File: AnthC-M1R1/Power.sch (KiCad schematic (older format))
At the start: 30 parts, among them Q8 SI2347DS-T1-GE3, Q9 SI2347DS-T1-GE3, U1 TPS54331DR, U3 TPS78533

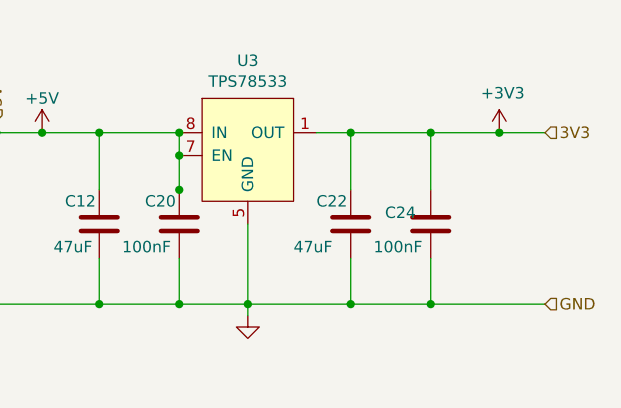
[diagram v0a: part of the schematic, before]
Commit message: Placement continued. Replaced quadrupled TVS by double ones to make routing easier
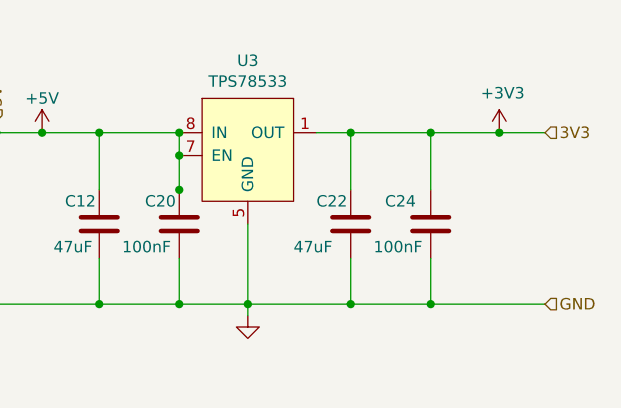
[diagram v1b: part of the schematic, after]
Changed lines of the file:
@@
 AR Path="/6251F79F" Ref="C?"  Part="1"
 AR Path="/6243F6D9/6251F79F" Ref="C24"  Part="1"
-F 0 "C24" H 9300 2050 50  0000 L CNN
+F 0 "C24" H 9300 2100 50  0000 L CNN
 F 1 "100nF" H 9250 1900 50  0000 L CNN
 F 2 "Capacitor_SMD:C_0603_1608Metric" H 10900 2200 50  0001 C CNN

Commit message: Placement continued
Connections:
- net GND: now also R2.2; no longer C7.2
- net at C5.1, U1.6 (COMP): now also C7.1; no longer R2.1
- new net: C7.2, R2.1
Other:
- moved on the sheet: C7, R2
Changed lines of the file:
@@
 AR Path="/6269B46A" Ref="R?"  Part="1"
 AR Path="/6243F6D9/6269B46A" Ref="R86"  Part="1"
-F 0 "R86" V 5800 2350 50  0000 L CNN
+F 0 "R86" V 5700 2300 50  0000 L CNN
 F 1 "8.2KΩ" H 5900 2300 50  0000 C CNN
 F 2 "Resistor_SMD:R_0603_1608Metric" H 5700 3350 50  0001 C CNN
@@
 L Resistor_0603:49.9 R?
 U 1 1 6269B4DA
-P 3600 2100
+P 3600 2300
 AR Path="/602E71BC/6269B4DA" Ref="R?"  Part="1"
 AR Path="/6269B4DA" Ref="R?"  Part="1"
 AR Path="/6243F6D9/6269B4DA" Ref="R2"  Part="1"
-F 0 "R2" H 3650 2200 50  0000 L CNN
-F 1 "49.9" H 3750 2050 50  0000 C CNN
-F 2 "Resistor_SMD:R_0603_1608Metric" H 3600 3100 50  0001 C CNN
-F 3 "https://www.mouser.be/datasheet/2/427/VISH_S_A0011410627_1-2571984.pdf" V 3250 2150 50  0001 C CNN
-F 4 "Vishay" H 3600 3425 50  0001 C CNN "Manufacturer"
-F 5 "33 kOhms ±1% 0.1W, 1/10W Chip Resistor 0603 (1608 Metric) Moisture Resistant Thick Film" H 3600 3025 50  0001 C CNN "Description"
-F 6 "TNPW020149R9BEED" H 3600 3225 50  0001 C CNN "Manufacturer Nr."
-F 7 "75mW" H 3600 3500 50  0001 C CNN "Power"
-F 8 "0.09" H 3600 2925 50  0001 C CNN "Price"
-F 9 "Mouser" H 3600 3325 50  0001 C CNN "Supplier"
-F 10 "71-TNPW020149R9BEED" H 3600 3625 50  0001 C CNN "Supplier Nr."
-F 11 "1%" H 3600 2850 50  0001 C CNN "Tolerance"
-F 12 "TNPW020149R9BEED" H 3600 2100 50  0001 C CNN "MPN"
-	1    3600 2100
+F 0 "R2" H 3650 2400 50  0000 L CNN
+F 1 "49.9" H 3750 2250 50  0000 C CNN
+F 2 "Resistor_SMD:R_0603_1608Metric" H 3600 3300 50  0001 C CNN
+F 3 "https://www.mouser.be/datasheet/2/427/VISH_S_A0011410627_1-2571984.pdf" V 3250 2350 50  0001 C CNN
+F 4 "Vishay" H 3600 3625 50  0001 C CNN "Manufacturer"
+F 5 "33 kOhms ±1% 0.1W, 1/10W Chip Resistor 0603 (1608 Metric) Moisture Resistant Thick Film" H 3600 3225 50  0001 C CNN "Description"
+F 6 "TNPW020149R9BEED" H 3600 3425 50  0001 C CNN "Manufacturer Nr."
+F 7 "75mW" H 3600 3700 50  0001 C CNN "Power"
+F 8 "0.09" H 3600 3125 50  0001 C CNN "Price"
+F 9 "Mouser" H 3600 3525 50  0001 C CNN "Supplier"
+F 10 "71-TNPW020149R9BEED" H 3600 3825 50  0001 C CNN "Supplier Nr."
+F 11 "1%" H 3600 3050 50  0001 C CNN "Tolerance"
+F 12 "TNPW020149R9BEED" H 3600 2300 50  0001 C CNN "MPN"
+	1    3600 2300
 	1    0    0    -1
 $EndComp
@@
 L Device:C_Small C?
 U 1 1 6269B4E3
-P 3600 2350
+P 3600 2050
 AR Path="/602E71BC/6269B4E3" Ref="C?"  Part="1"
 AR Path="/6269B4E3" Ref="C?"  Part="1"
 AR Path="/6243F6D9/6269B4E3" Ref="C7"  Part="1"
-F 0 "C7" H 3692 2396 50  0000 L CNN
-F 1 "4.7nF" H 3692 2305 50  0000 L CNN
-F 2 "Capacitor_SMD:C_0402_1005Metric" H 3600 2350 50  0001 C CNN
-F 3 "~" H 3600 2350 50  0001 C CNN
-F 4 "C1538" H 3600 2350 50  0001 C CNN "LCSC-PN"
-F 5 "0402B472K500NT" H 3600 2350 50  0001 C CNN "MPN"
-F 6 "Guangdong Fenghua Advanced Tech" H 3600 2350 50  0001 C CNN "Manufacturer"
-	1    3600 2350
-	1    0    0    -1
-$EndComp
+F 0 "C7" H 3692 2096 50  0000 L CNN
+F 1 "4.7nF" H 3692 2005 50  0000 L CNN
+F 2 "Capacitor_SMD:C_0402_1005Metric" H 3600 2050 50  0001 C CNN
+F 3 "~" H 3600 2050 50  0001 C CNN
+F 4 "C1538" H 3600 2050 50  0001 C CNN "LCSC-PN"
+F 5 "0402B472K500NT" H 3600 2050 50  0001 C CNN "MPN"
+F 6 "Guangdong Fenghua Advanced Tech" H 3600 2050 50  0001 C CNN "Manufacturer"
+	1    3600 2050
+	1    0    0    -1
+$EndComp

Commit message: Placement continued
Replaced L1 by another inductance that supports 3A
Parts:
- L1: value 10μH -> 10μH-5A; footprint Inductors:Inductor_Wurth_LQS-4025 -> Inductors:Inductor_Wurth_XHMI-6060; symbol Inductors:10μH -> Inductors:10μH-5A; MPN 74404043100A -> 74439346100; Price 0.435 -> (none); Supplier Part Number 710-74404043100A -> 710-74439346100
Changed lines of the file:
@@
 $EndComp
 $Comp
-L Inductors:10μH L?
+L Inductors:10μH-5A L?
 U 1 1 6269B54A
 P 5000 1600
@@
 AR Path="/6243F6D9/6269B54A" Ref="L1"  Part="1"
 F 0 "L1" V 5190 1600 50  0000 C CNN
-F 1 "10μH" V 5075 1600 50  0000 C CNN
-F 2 "Inductors:Inductor_Wurth_LQS-4025" H 5000 1600 50  0001 C CNN
-F 3 "https://www.we-online.com/catalog/datasheet/74404043100A.pdf" H 5000 1600 50  0001 C CNN
-F 4 "74404043100A" H 6200 2050 50  0001 C CNN "MPN"
+F 1 "10μH-5A" V 5075 1600 50  0000 C CNN
+F 2 "Inductors:Inductor_Wurth_XHMI-6060" H 5000 1600 50  0001 C CNN
+F 3 "https://www.we-online.com/catalog/datasheet/74439346100.pdf" H 5000 1600 50  0001 C CNN
+F 4 "74439346100" H 6200 2050 50  0001 C CNN "MPN"
 F 5 "Wurth Elektronik" H 5500 2050 50  0001 C CNN "Manufacturer"
-F 6 "0.435" H 5350 1850 50  0001 C CNN "Price"
-F 7 "Mouser" H 5350 1950 50  0001 C CNN "Supplier"
-F 8 "710-74404043100A" H 6300 1950 50  0001 C CNN "Supplier Part Number"
+F 6 "Mouser" H 5350 1950 50  0001 C CNN "Supplier"
+F 7 "710-74439346100" H 6300 1950 50  0001 C CNN "Supplier Part Number"
 	1    5000 1600
 	0    -1   -1   0

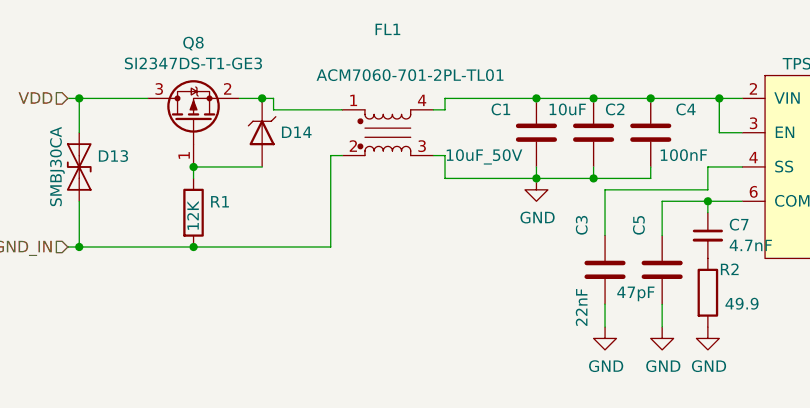
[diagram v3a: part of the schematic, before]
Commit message: Routing continued Changed the order of the connector J5 to improve routing
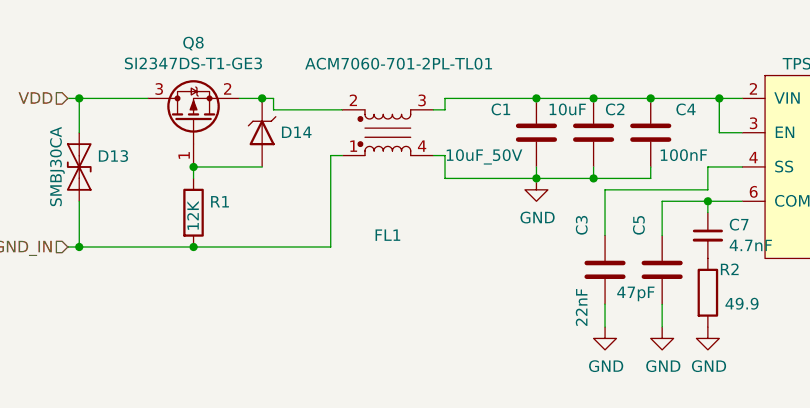
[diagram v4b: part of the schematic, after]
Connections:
- net GND: now also FL1.4; no longer FL1.3
- net GND_IN: now also FL1.1; no longer FL1.2
- net at D14.1 (K), Q8.2 (S): now also FL1.2; no longer FL1.1
- net at C1.1, C2.1, C4.1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: now also FL1.3; no longer FL1.4
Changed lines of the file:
@@
 L Inductors:ACM7060-701-2PL-TL01 FL1
 U 1 1 6236793A
-P 2000 1700
-F 0 "FL1" H 2200 2250 50  0000 C CNN
-F 1 "ACM7060-701-2PL-TL01" H 2300 2050 50  0000 C CNN
-F 2 "Inductors:ChokeSMD_ACM7060" H 2000 3050 50  0001 C CNN
-F 3 "https://product.tdk.com/system/files/dam/doc/product/emc/emc/cmf_cmc/catalog/cmf_commercial_power_acm7060_en.pdf" V 2200 1760 50  0001 C CNN
-F 4 "Common Mode Chokes / Filters 700ohms 100MHz 50volts" H 2000 2950 50  0001 C CNN "Description"
-F 5 "TDK" H 2000 2850 50  0001 C CNN "Manufacturer"
-F 6 "ACM7060-701-2PL-TL01" H 2000 2750 50  0001 C CNN "Manufacturer Nr."
-F 7 "Mouser" H 2000 2650 50  0001 C CNN "Supplier"
-F 8 "810-ACM70607012PLTL1" H 2000 2550 50  0001 C CNN "Supplier Nr."
-	1    2000 1700
-	1    0    0    -1
+P 2000 1500
+F 0 "FL1" H 2200 2050 50  0000 C CNN
+F 1 "ACM7060-701-2PL-TL01" H 2250 1300 50  0000 C CNN
+F 2 "Inductors:ChokeSMD_ACM7060" H 2000 2850 50  0001 C CNN
+F 3 "https://product.tdk.com/system/files/dam/doc/product/emc/emc/cmf_cmc/catalog/cmf_commercial_power_acm7060_en.pdf" V 2200 1560 50  0001 C CNN
+F 4 "Common Mode Chokes / Filters 700ohms 100MHz 50volts" H 2000 2750 50  0001 C CNN "Description"
+F 5 "TDK" H 2000 2650 50  0001 C CNN "Manufacturer"
+F 6 "ACM7060-701-2PL-TL01" H 2000 2550 50  0001 C CNN "Manufacturer Nr."
+F 7 "Mouser" H 2000 2450 50  0001 C CNN "Supplier"
+F 8 "810-ACM70607012PLTL1" H 2000 2350 50  0001 C CNN "Supplier Nr."
+	1    2000 1500
+	1    0    0    1
 $EndComp
 Wire Wire Line

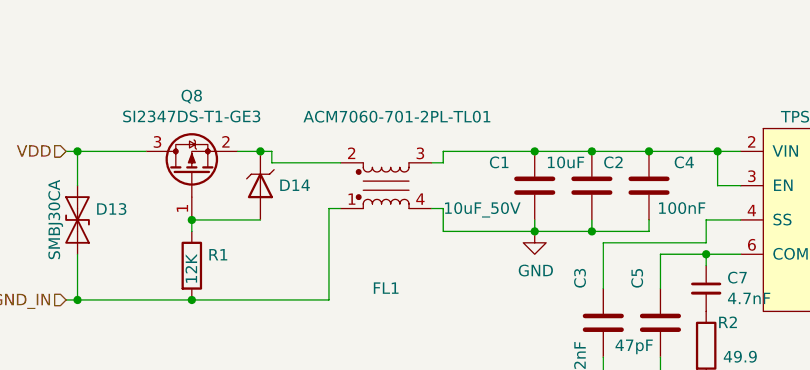
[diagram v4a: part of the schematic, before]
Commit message: Layout continued. Verified USB-C. Corrected layout of the TPS DC/DC converter
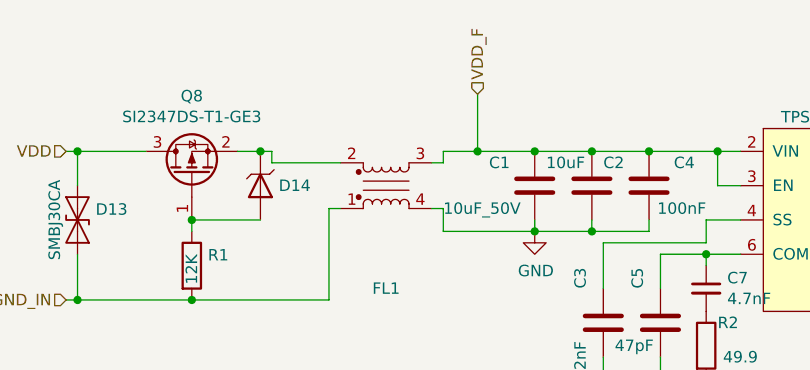
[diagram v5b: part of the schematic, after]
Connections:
- net VDD_F: now reaches C1.1, C2.1, C4.1, FL1.3, U1.2 (VIN), U1.3 (EN)
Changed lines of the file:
@@
 P 2000 1500
 F 0 "FL1" H 2200 2050 50  0000 C CNN
-F 1 "ACM7060-701-2PL-TL01" H 2250 1300 50  0000 C CNN
+F 1 "ACM7060-701-2PL-TL01" H 2250 1300 50  0001 C CNN
 F 2 "Inductors:ChokeSMD_ACM7060" H 2000 2850 50  0001 C CNN
 F 3 "https://product.tdk.com/system/files/dam/doc/product/emc/emc/cmf_cmc/catalog/cmf_commercial_power_acm7060_en.pdf" V 2200 1560 50  0001 C CNN
@@
 	2450 1500 2450 1450
 Wire Wire Line
-	2450 1450 2850 1450
+	2450 1450 2600 1450
 Wire Wire Line
 	2400 1500 2450 1500
@@
 Wire Wire Line
 	1350 2100 1950 2100
+Text HLabel 2600 1200 1    50   Input ~ 0
+VDD_F
+Wire Wire Line
+	2600 1450 2600 1200
+Connection ~ 2600 1450
+Wire Wire Line
+	2600 1450 2850 1450
 $EndSCHEMATC

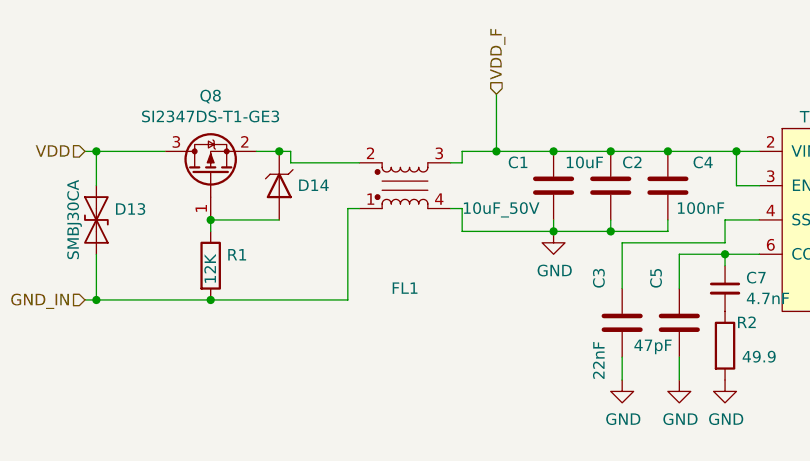
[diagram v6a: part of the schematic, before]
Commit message: Updated BOM info: added MPN to all the components
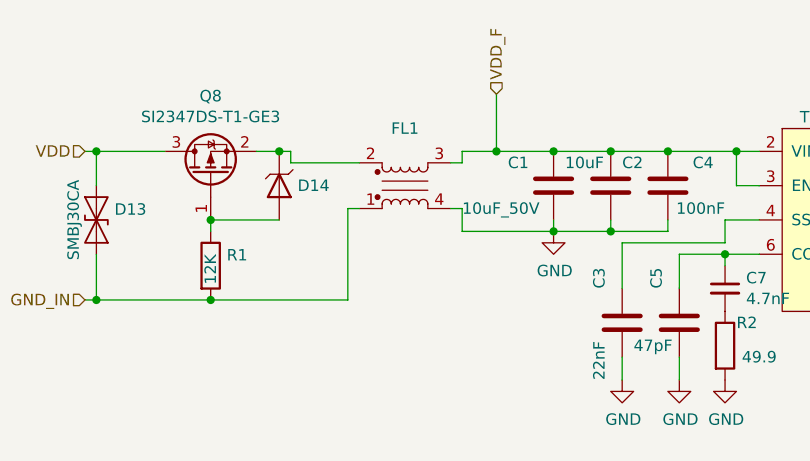
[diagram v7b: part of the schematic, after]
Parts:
- D13: MPN (none) -> SMBJ30CA; Manufacturer Part Number SMBJ30CA -> (none)
- D14, D24: MPN (none) -> MMSZ5233B-E3-08; Manufacturer Part Number MMSZ5233B-E3-08 -> (none)
- FL1: MPN (none) -> ACM7060-701-2PL-TL01; Manufacturer Nr. ACM7060-701-2PL-TL01 -> (none)
- Q8, Q9: MPN (none) -> SI2347DS-T1-GE3; Manufacturer Nr. SI2347DS-T1-GE3 -> (none)
- R1, R87: MPN (none) -> RT0603FRE0712KL; Manufacturer Part Number RT0603FRE0712KL -> (none)
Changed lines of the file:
@@
 F 4 "Suppresseurs ESD / diodes TVS 600W 30V 5% Bi-Directional" H 850 2900 50  0001 C CNN "Description"
 F 5 "Littelfuse" H 850 2800 50  0001 C CNN "Manufacturer"
-F 6 "SMBJ30CA" H 850 2700 50  0001 C CNN "Manufacturer Part Number"
-F 7 "Mouser" H 850 1750 50  0001 C CNN "Supplier"
-F 8 "576-SMBJ30CA" H 850 1750 50  0001 C CNN "Supplier Part Number"
+F 6 "Mouser" H 850 1750 50  0001 C CNN "Supplier"
+F 7 "576-SMBJ30CA" H 850 1750 50  0001 C CNN "Supplier Part Number"
+F 8 "SMBJ30CA" H 850 2700 50  0001 C CNN "MPN"
 	1    850  1750
 	0    1    1    0
@@
 U 1 1 6236793A
 P 2000 1500
-F 0 "FL1" H 2200 2050 50  0000 C CNN
+F 0 "FL1" H 2200 1350 50  0000 C CNN
 F 1 "ACM7060-701-2PL-TL01" H 2250 1300 50  0001 C CNN
 F 2 "Inductors:ChokeSMD_ACM7060" H 2000 2850 50  0001 C CNN
@@
 F 4 "Common Mode Chokes / Filters 700ohms 100MHz 50volts" H 2000 2750 50  0001 C CNN "Description"
 F 5 "TDK" H 2000 2650 50  0001 C CNN "Manufacturer"
-F 6 "ACM7060-701-2PL-TL01" H 2000 2550 50  0001 C CNN "Manufacturer Nr."
-F 7 "Mouser" H 2000 2450 50  0001 C CNN "Supplier"
-F 8 "810-ACM70607012PLTL1" H 2000 2350 50  0001 C CNN "Supplier Nr."
+F 6 "Mouser" H 2000 2450 50  0001 C CNN "Supplier"
+F 7 "810-ACM70607012PLTL1" H 2000 2350 50  0001 C CNN "Supplier Nr."
+F 8 "ACM7060-701-2PL-TL01" H 2000 1500 50  0001 C CNN "MPN"
 	1    2000 1500
 	1    0    0    1
@@
 F 4 "MOSFET -30V Vds 20V Vgs SOT-23" H 1350 2850 50  0001 C CNN "Description"
 F 5 "Vishay Semiconductors" H 1350 2750 50  0001 C CNN "Manufacturer"
-F 6 "SI2347DS-T1-GE3" H 1350 2650 50  0001 C CNN "Manufacturer Nr."
-F 7 "Mouser" H 1350 2550 50  0001 C CNN "Supplier"
-F 8 "78-SI2347DS-T1-GE3" H 1350 2450 50  0001 C CNN "Supplier Nr."
+F 6 "Mouser" H 1350 2550 50  0001 C CNN "Supplier"
+F 7 "78-SI2347DS-T1-GE3" H 1350 2450 50  0001 C CNN "Supplier Nr."
+F 8 "SI2347DS-T1-GE3" H 1350 1450 50  0001 C CNN "MPN"
 	1    1350 1450
 	0    -1   -1   0
@@
 F 3 "https://www.mouser.be/datasheet/2/427/VISH_S_A0003941535_1-2569124.pdf" H 1650 1600 50  0001 C CNN
 F 4 "Vishay" H 1950 2200 50  0001 C CNN "Manufacturer"
-F 5 "MMSZ5233B-E3-08" H 2550 2200 50  0001 C CNN "Manufacturer Part Number"
-F 6 "Mouser" H 1950 2100 50  0001 C CNN "Supplier"
-F 7 "78-MMSZ5233B-E3-08" H 2650 2100 50  0001 C CNN "Supplier Part Number"
-F 8 "6V" H 2250 1900 50  0001 C CNN "Voltage"
-F 9 "500mW" H 2350 2000 50  0001 C CNN "Power"
+F 5 "Mouser" H 1950 2100 50  0001 C CNN "Supplier"
+F 6 "78-MMSZ5233B-E3-08" H 2650 2100 50  0001 C CNN "Supplier Part Number"
+F 7 "6V" H 2250 1900 50  0001 C CNN "Voltage"
+F 8 "500mW" H 2350 2000 50  0001 C CNN "Power"
+F 9 "MMSZ5233B-E3-08" H 1650 1600 50  0001 C CNN "MPN"
 	1    1650 1600
 	0    1    1    0
@@
 F 3 "https://www.mouser.be/datasheet/2/427/VISH_S_A0003941535_1-2569124.pdf" H 7200 1750 50  0001 C CNN
 F 4 "Vishay" H 7500 2350 50  0001 C CNN "Manufacturer"
-F 5 "MMSZ5233B-E3-08" H 8100 2350 50  0001 C CNN "Manufacturer Part Number"
-F 6 "Mouser" H 7500 2250 50  0001 C CNN "Supplier"
-F 7 "78-MMSZ5233B-E3-08" H 8200 2250 50  0001 C CNN "Supplier Part Number"
-F 8 "6V" H 7800 2050 50  0001 C CNN "Voltage"
-F 9 "500mW" H 7900 2150 50  0001 C CNN "Power"
+F 5 "Mouser" H 7500 2250 50  0001 C CNN "Supplier"
+F 6 "78-MMSZ5233B-E3-08" H 8200 2250 50  0001 C CNN "Supplier Part Number"
+F 7 "6V" H 7800 2050 50  0001 C CNN "Voltage"
+F 8 "500mW" H 7900 2150 50  0001 C CNN "Power"
+F 9 "MMSZ5233B-E3-08" H 7200 1750 50  0001 C CNN "MPN"
 	1    7200 1750
 	0    1    1    0
@@
 F 5 "Mouser" H 6900 3000 50  0001 C CNN "Supplier"
 F 6 "12 kOhms ±1% 0.1W, 1/10W Chip Resistor 0603 (1608 Metric)  Thin Film" H 6900 3300 50  0001 C CNN "Description"
-F 7 "RT0603FRE0712KL" H 6900 3100 50  0001 C CNN "Manufacturer Part Number"
-F 8 "603-RT0603FRE0712KL" H 6900 2900 50  0001 C CNN "Supplier Part Number"
+F 7 "603-RT0603FRE0712KL" H 6900 2900 50  0001 C CNN "Supplier Part Number"
+F 8 "RT0603FRE0712KL" H 6900 2150 50  0001 C CNN "MPN"
 	1    6900 2150
 	0    1    1    0
@@
 F 4 "MOSFET -30V Vds 20V Vgs SOT-23" H 6900 3000 50  0001 C CNN "Description"
 F 5 "Vishay Semiconductors" H 6900 2900 50  0001 C CNN "Manufacturer"
-F 6 "SI2347DS-T1-GE3" H 6900 2800 50  0001 C CNN "Manufacturer Nr."
-F 7 "Mouser" H 6900 2700 50  0001 C CNN "Supplier"
-F 8 "78-SI2347DS-T1-GE3" H 6900 2600 50  0001 C CNN "Supplier Nr."
+F 6 "Mouser" H 6900 2700 50  0001 C CNN "Supplier"
+F 7 "78-SI2347DS-T1-GE3" H 6900 2600 50  0001 C CNN "Supplier Nr."
+F 8 "SI2347DS-T1-GE3" H 6900 1600 50  0001 C CNN "MPN"
 	1    6900 1600
 	0    -1   -1   0
@@
 F 3 "https://www.mouser.es/datasheet/2/447/PYu-RT_1-to-0.01_RoHS_L_11-1669912.pdf" V 1000 2000 50  0001 C CNN
 F 4 "Yageo" H 1350 3000 50  0001 C CNN "Manufacturer"
-F 5 "RT0603FRE0712KL" H 1350 2900 50  0001 C CNN "Manufacturer Part Number"
-F 6 "Mouser" H 1350 2800 50  0001 C CNN "Supplier"
-F 7 "603-RT0603FRE0712KL" H 1350 2700 50  0001 C CNN "Supplier Part Number"
-F 8 "12 kOhms ±1% 0.1W, 1/10W Chip Resistor 0603 (1608 Metric)  Thin Film" H 1350 3100 50  0001 C CNN "Description"
+F 5 "Mouser" H 1350 2800 50  0001 C CNN "Supplier"
+F 6 "603-RT0603FRE0712KL" H 1350 2700 50  0001 C CNN "Supplier Part Number"
+F 7 "12 kOhms ±1% 0.1W, 1/10W Chip Resistor 0603 (1608 Metric)  Thin Film" H 1350 3100 50  0001 C CNN "Description"
+F 8 "RT0603FRE0712KL" H 1350 1950 50  0001 C CNN "MPN"
 	1    1350 1950
 	0    1    1    0
